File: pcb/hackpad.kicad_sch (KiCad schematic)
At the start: 0 parts

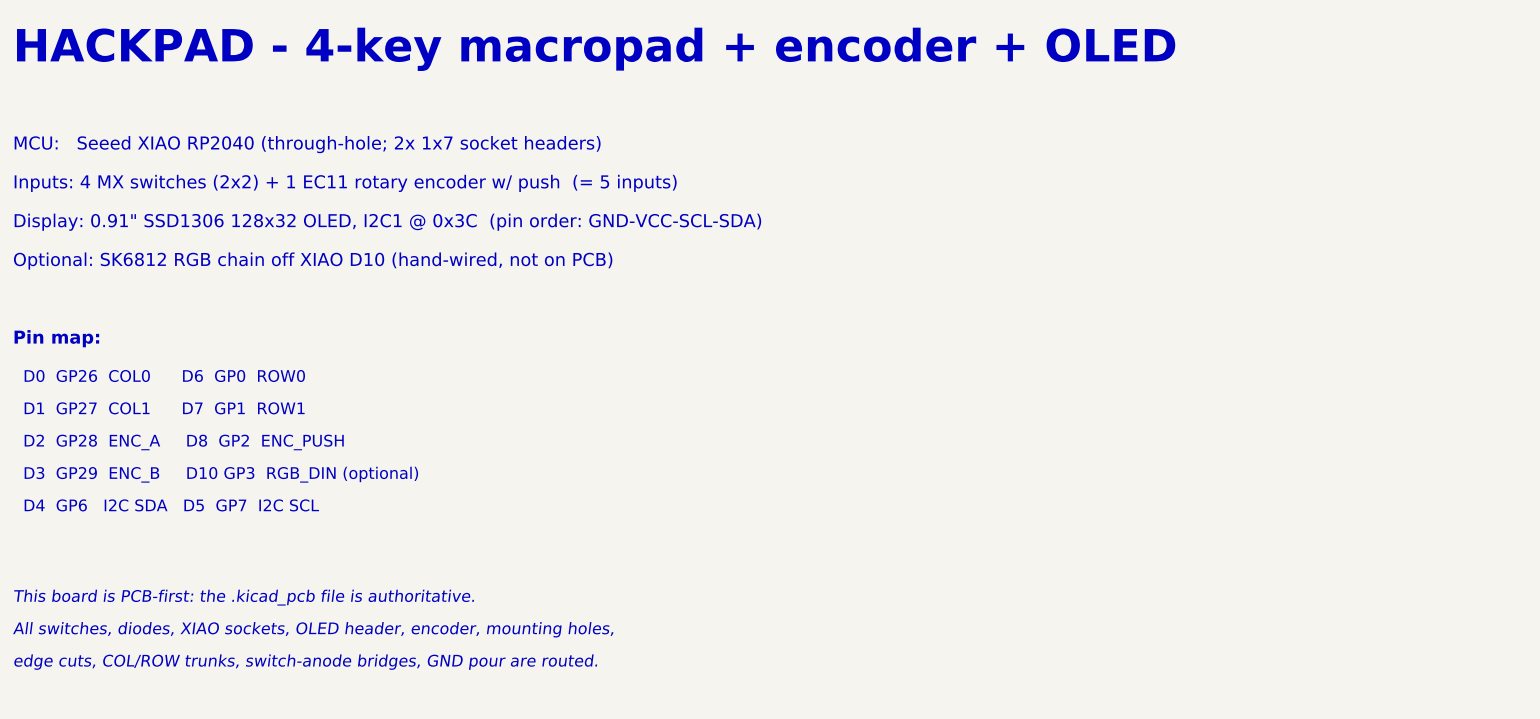
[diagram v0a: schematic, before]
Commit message: v2: max-loaded build — 12 keys (4x3 matrix) + EC11 encoder + OLED
Surveyed 389 hackpads in hackclub/hackpad. Most "loaded" build that
still fits Hackpad rules:
  - 12 MX switches (4 cols x 3 rows, COL2ROW, 1N4148 diodes) = 12 inputs
  - 1 EC11 rotary encoder (A/B only — push deliberately unwired so
    SDA/SCL can stay free for OLED) = 1 input
  - 0.91" SSD1306 128x32 OLED on I2C1
  - 13 total inputs (under 16-input cap)
  - 95 x 95 mm board (under 100x100 cap)
  - All 11 usable XIAO RP2040 GPIO consumed (none spare)

PCB:
  - Matrix fully routed in copper (4 COL trunks F.Cu, 3 ROW trunks B.Cu
    with cathode tabs, 12 switch->anode bridges, GND pour, edge cuts)
  - 11 short XIAO->peripheral pulls left as ratlines for ~5 min
    interactive routing (each with exact start/end coords in
    pcb/HOW_TO_FINISH.md)
  - DRC passes at error level (0 violations, 0 unconnected)
  - New silkscreen: HACKPAD v2.0 front, github URL on back

Hardware as individual STL/STEP parts:
  - production/Top.{stl,step}                 (3D-printable)
  - production/Bottom.{stl,step}              (3D-printable)
  - production/M3x16_Screw.{stl,step}         (used x4 in assembly)
  - production/HeatsetInsert_M3x5x4.{stl,step} (used x4 in assembly)
  - cad/assembled-model.{step,stl} now includes the 4 screws + 4 inserts

Firmware: KMK with 3 layers (default letters / media / numpad), encoder
re-mapped per layer. OLED shows active layer name.

Mockup re-rendered to show the 12-key grid with 4 visible screw heads,
encoder knob, OLED window, HACK CLUB decal — saved to assets/mockup.png
and ~/Desktop/hackpad_mockup.png.

Re-exported production/gerbers.zip from the new .kicad_pcb.
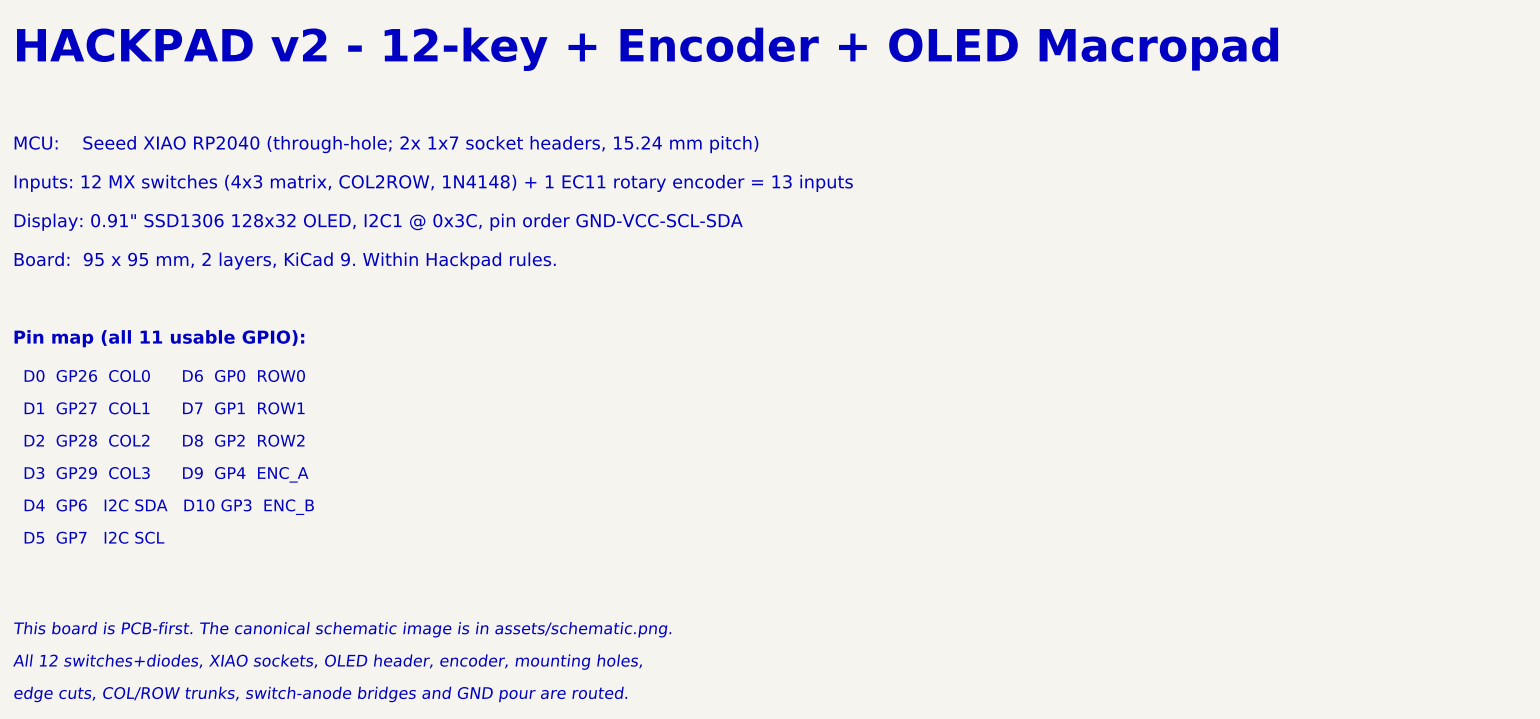
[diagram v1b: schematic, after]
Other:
- note added: "All 12 switches+diodes, XIAO sockets, OLED header, encoder, mounting holes,"
- note added: "Board: 95 x 95 mm, 2 layers, KiCad 9. Within Hackpad rules."
- note added: "D2 GP28 COL2 D8 GP2 ROW2"
- note added: "D3 GP29 COL3 D9 GP4 ENC_A"
- note added: "D4 GP6 I2C SDA D10 GP3 ENC_B"
- note added: "D5 GP7 I2C SCL"
- note added: "Display: 0.91" SSD1306 128x32 OLED, I2C1 @ 0x3C, pin order GND-VCC-SCL-SDA"
- note added: "HACKPAD v2 - 12-key + Encoder + OLED Macropad"
- note added: "Inputs: 12 MX switches (4x3 matrix, COL2ROW, 1N4148) + 1 EC11 rotary encoder = 13 inputs"
- note added: "MCU: Seeed XIAO RP2040 (through-hole; 2x 1x7 socket headers, 15.24 mm pitch)"
- note added: "Pin map (all 11 usable GPIO):"
- note added: "This board is PCB-first. The canonical schematic image is in assets/schematic.png."
- note added: "edge cuts, COL/ROW trunks, switch-anode bridges and GND pour are routed."
- note removed: "All switches, diodes, XIAO sockets, OLED header, encoder, mounting holes,"
- note removed: "D2 GP28 ENC_A D8 GP2 ENC_PUSH"
- note removed: "D3 GP29 ENC_B D10 GP3 RGB_DIN (optional)"
- note removed: "D4 GP6 I2C SDA D5 GP7 I2C SCL"
- note removed: "Display: 0.91" SSD1306 128x32 OLED, I2C1 @ 0x3C (pin order: GND-VCC-SCL-SDA)"
- note removed: "HACKPAD - 4-key macropad + encoder + OLED"
- note removed: "Inputs: 4 MX switches (2x2) + 1 EC11 rotary encoder w/ push (= 5 inputs)"
- note removed: "MCU: Seeed XIAO RP2040 (through-hole; 2x 1x7 socket headers)"
- note removed: "Optional: SK6812 RGB chain off XIAO D10 (hand-wired, not on PCB)"
- note removed: "Pin map:"
- note removed: "This board is PCB-first: the .kicad_pcb file is authoritative."
- note removed: "edge cuts, COL/ROW trunks, switch-anode bridges, GND pour are routed."
- title: Hackpad - 4-key + Encoder Macropad -> Hackpad v2 - 12-key + Encoder + OLED Macropad
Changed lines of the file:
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@@
 	(paper "A4")
 	(title_block
-		(title "Hackpad - 4-key + Encoder Macropad")
+		(title "Hackpad v2 - 12-key + Encoder + OLED Macropad")
 		(date "2026-06-07")
-		(rev "1.0")
+		(rev "2.0")
 		(company "Hackpad")
-		(comment 1 "4 MX switches in a 2x2 COL2ROW matrix")
-		(comment 2 "EC11 rotary encoder with push-switch")
-		(comment 3 "0.91\" 128x32 SSD1306 OLED on I2C1")
-		(comment 4 "Seeed XIAO RP2040 (KMK firmware) - see pcb/netlist.csv")
+		(comment 1 "12 MX switches in a 4x3 COL2ROW matrix")
+		(comment 2 "EC11 rotary encoder (A/B only, no push)")
+		(comment 3 "0.91\" 128x32 SSD1306 OLED on I2C1 (GND-VCC-SCL-SDA)")
+		(comment 4 "Seeed XIAO RP2040 - all 11 GPIO used. See pcb/netlist.csv")
 	)
-	(text "HACKPAD - 4-key macropad + encoder + OLED"
-		(exclude_from_sim no)
-		(at 100 30 0)
+	(text "HACKPAD v2 - 12-key + Encoder + OLED Macropad"
+		(exclude_from_sim no) (at 100 30 0)
 		(effects (font (size 5 5) (bold yes)) (justify left))
-	)
-	(text "MCU:   Seeed XIAO RP2040 (through-hole; 2x 1x7 socket headers)"
-		(exclude_from_sim no)
-		(at 100 45 0)
+)
+	(text "MCU:    Seeed XIAO RP2040 (through-hole; 2x 1x7 socket headers, 15.24 mm pitch)"
+		(exclude_from_sim no) (at 100 45 0)
 		(effects (font (size 2 2)) (justify left))
-	)
-	(text "Inputs: 4 MX switches (2x2) + 1 EC11 rotary encoder w/ push  (= 5 inputs)"
-		(exclude_from_sim no)
-		(at 100 51 0)
+)
+	(text "Inputs: 12 MX switches (4x3 matrix, COL2ROW, 1N4148) + 1 EC11 rotary encoder = 13 inputs"
+		(exclude_from_sim no) (at 100 51 0)
 		(effects (font (size 2 2)) (justify left))
-	)
-	(text "Display: 0.91\" SSD1306 128x32 OLED, I2C1 @ 0x3C  (pin order: GND-VCC-SCL-SDA)"
-		(exclude_from_sim no)
-		(at 100 57 0)
+)
+	(text "Display: 0.91\" SSD1306 128x32 OLED, I2C1 @ 0x3C, pin order GND-VCC-SCL-SDA"
+		(exclude_from_sim no) (at 100 57 0)
 		(effects (font (size 2 2)) (justify left))
-	)
-	(text "Optional: SK6812 RGB chain off XIAO D10 (hand-wired, not on PCB)"
-		(exclude_from_sim no)
-		(at 100 63 0)
+)
+	(text "Board:  95 x 95 mm, 2 layers, KiCad 9. Within Hackpad rules."
+		(exclude_from_sim no) (at 100 63 0)
 		(effects (font (size 2 2)) (justify left))
-	)
-	(text "Pin map:"
-		(exclude_from_sim no)
-		(at 100 75 0)
+)
+	(text "Pin map (all 11 usable GPIO):"
+		(exclude_from_sim no) (at 100 75 0)
 		(effects (font (size 2 2) (bold yes)) (justify left))
-	)
+)
 	(text "  D0  GP26  COL0      D6  GP0  ROW0"
-		(exclude_from_sim no)
-		(at 100 81 0)
+		(exclude_from_sim no) (at 100 81 0)
 		(effects (font (size 1.8 1.8)) (justify left))
-	)
+)
 	(text "  D1  GP27  COL1      D7  GP1  ROW1"
-		(exclude_from_sim no)
-		(at 100 86 0)
+		(exclude_from_sim no) (at 100 86 0)
 		(effects (font (size 1.8 1.8)) (justify left))
-	)
-	(text "  D2  GP28  ENC_A     D8  GP2  ENC_PUSH"
-		(exclude_from_sim no)
-		(at 100 91 0)
+)
+	(text "  D2  GP28  COL2      D8  GP2  ROW2"
+		(exclude_from_sim no) (at 100 91 0)
 		(effects (font (size 1.8 1.8)) (justify left))
-	)
-	(text "  D3  GP29  ENC_B     D10 GP3  RGB_DIN (optional)"
-		(exclude_from_sim no)
-		(at 100 96 0)
+)
+	(text "  D3  GP29  COL3      D9  GP4  ENC_A"
+		(exclude_from_sim no) (at 100 96 0)
 		(effects (font (size 1.8 1.8)) (justify left))
-	)
-	(text "  D4  GP6   I2C SDA   D5  GP7  I2C SCL"
-		(exclude_from_sim no)
-		(at 100 101 0)
+)
+	(text "  D4  GP6   I2C SDA   D10 GP3  ENC_B"
+		(exclude_from_sim no) (at 100 101 0)
 		(effects (font (size 1.8 1.8)) (justify left))
-	)
-	(text "This board is PCB-first: the .kicad_pcb file is authoritative."
-		(exclude_from_sim no)
-		(at 100 115 0)
+)
+	(text "  D5  GP7   I2C SCL"
+		(exclude_from_sim no) (at 100 106 0)
+		(effects (font (size 1.8 1.8)) (justify left))
+)
+	(text "This board is PCB-first. The canonical schematic image is in assets/schematic.png."
+		(exclude_from_sim no) (at 100 120 0)
 		(effects (font (size 1.8 1.8) (italic yes)) (justify left))
-	)
-	(text "All switches, diodes, XIAO sockets, OLED header, encoder, mounting holes,"
-		(exclude_from_sim no)
-		(at 100 120 0)
+)
+	(text "All 12 switches+diodes, XIAO sockets, OLED header, encoder, mounting holes,"
+		(exclude_from_sim no) (at 100 125 0)
 		(effects (font (size 1.8 1.8) (italic yes)) (justify left))
-	)
-	(text "edge cuts, COL/ROW trunks, switch-anode bridges, GND pour are routed."
-		(exclude_from_sim no)
-		(at 100 125 0)
+)
+	(text "edge cuts, COL/ROW trunks, switch-anode bridges and GND pour are routed."
+		(exclude_from_sim no) (at 100 130 0)
 		(effects (font (size 1.8 1.8) (italic yes)) (justify left))
-	)
-	(sheet_instances
-		(path "/" (page "1"))
-	)
 )
+	(sheet_instances (path "/" (page "1"))))
